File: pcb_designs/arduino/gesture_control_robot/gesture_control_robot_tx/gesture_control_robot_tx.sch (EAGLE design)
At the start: 21 parts, among them IC1 ATMEGA328, IC2 7805, Q1 16MHZ

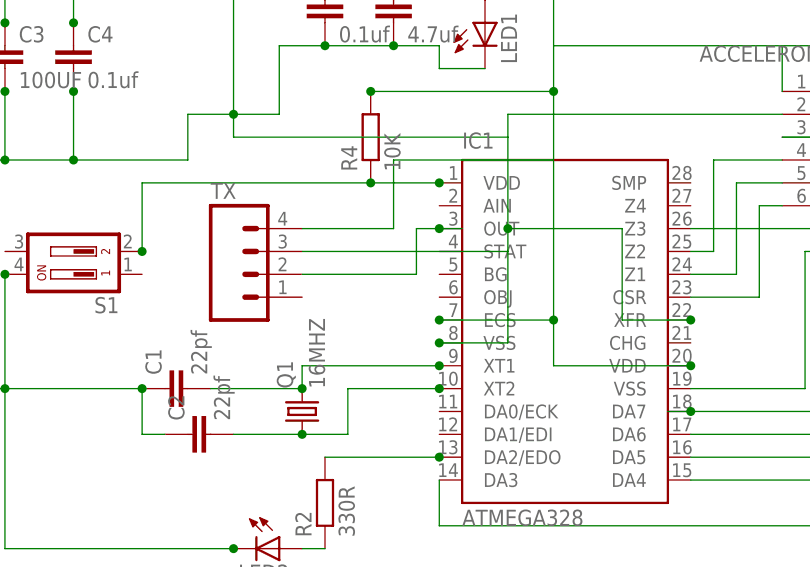
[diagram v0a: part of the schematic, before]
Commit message: 
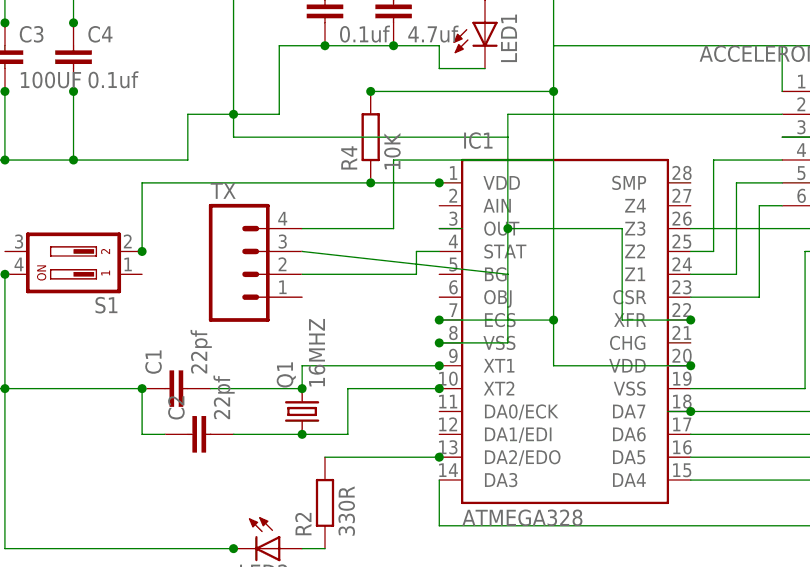
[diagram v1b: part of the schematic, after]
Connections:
- new net N$12: IC1.OUT
- net N$13: now also IC1.STAT; no longer IC1.OUT
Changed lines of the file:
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@@
 <pinref part="IC1" gate="G$1" pin="VSS"/>
 <wire x1="-5.08" y1="81.28" x2="2.54" y2="81.28" width="0.1524" layer="91"/>
-<wire x1="2.54" y1="81.28" x2="2.54" y2="91.44" width="0.1524" layer="91"/>
+<wire x1="2.54" y1="81.28" x2="2.54" y2="88.9" width="0.1524" layer="91"/>
 <junction x="-5.08" y="81.28"/>
 <junction x="2.54" y="93.98"/>
-<wire x1="2.54" y1="91.44" x2="2.54" y2="93.98" width="0.1524" layer="91"/>
+<wire x1="2.54" y1="88.9" x2="2.54" y2="93.98" width="0.1524" layer="91"/>
 <wire x1="-27.94" y1="121.92" x2="-27.94" y2="137.16" width="0.1524" layer="91"/>
 <pinref part="LCD" gate="G$1" pin="1"/>
@@
 <wire x1="2.54" y1="106.68" x2="2.54" y2="104.14" width="0.1524" layer="91"/>
 <pinref part="TX" gate="G$1" pin="3"/>
-<wire x1="-20.32" y1="91.44" x2="2.54" y2="91.44" width="0.1524" layer="91"/>
+<wire x1="-20.32" y1="91.44" x2="2.54" y2="88.9" width="0.1524" layer="91"/>
 </segment>
 </net>
@@
 </segment>
 </net>
+<net name="N$12" class="0">
+<segment>
+<pinref part="IC1" gate="G$1" pin="OUT"/>
+<wire x1="-5.08" y1="93.98" x2="-2.54" y2="93.98" width="0.1524" layer="91"/>
+</segment>
+</net>
 <net name="N$13" class="0">
 <segment>
 <pinref part="TX" gate="G$1" pin="2"/>
 <wire x1="-20.32" y1="88.9" x2="-7.62" y2="88.9" width="0.1524" layer="91"/>
-<wire x1="-7.62" y1="88.9" x2="-7.62" y2="93.98" width="0.1524" layer="91"/>
-<wire x1="-7.62" y1="93.98" x2="-5.08" y2="93.98" width="0.1524" layer="91"/>
-<pinref part="IC1" gate="G$1" pin="OUT"/>
-<junction x="-5.08" y="93.98"/>
-<wire x1="-5.08" y1="93.98" x2="-2.54" y2="93.98" width="0.1524" layer="91"/>
-</segment>
-</net>
+<wire x1="-7.62" y1="88.9" x2="-7.62" y2="91.44" width="0.1524" layer="91"/>
+<pinref part="IC1" gate="G$1" pin="STAT"/>
+<wire x1="-7.62" y1="91.44" x2="-5.08" y2="91.44" width="0.1524" layer="91"/>
+</segment>
+</net>
